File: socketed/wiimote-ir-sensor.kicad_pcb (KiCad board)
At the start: 2 copper layers, 13.5 x 16.2 mm, 10 parts, among them J1 Conn_01x04_Pin, U2 AP2112-3.3V, X1 SG3225CAN 24.0000M-TJGA3

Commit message: Socketed board: Tidy up
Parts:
- moved C1 22.8 mm to (158.2, 110.2)
- moved U1 22.0 mm to (156.8, 102.8)
- moved C3 22.0 mm to (152.0, 108.8)
- moved R1 22.0 mm to (154.8, 110.2)
- moved R2 22.0 mm to (156.5, 110.2)
- moved R3 22.0 mm to (161.0, 108.8)
- moved U2 22.0 mm to (151.9, 110.1)
- moved X1 22.0 mm to (159.5, 109.6)
- moved J1 21.7 mm to (152.9, 114.2)
- moved C2 21.7 mm to (152.0, 111.4)
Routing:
- net GND: track 30.5 -> 44.8 mm, vias 1 -> 6
- net +5V: track 11.7 -> 10.2 mm
- net /SCL: track 29.0 -> 27.7 mm
- net /CLK: track 17.2 -> 16.6 mm
- net /SDA: track 14.3 -> 14.7 mm, vias 2 -> 1

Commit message: More QoL tweaks to socketed board
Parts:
- R3: value 330K -> 33K
- moved J1 7.62 mm to (160.6, 114.2), turned to -90 degrees
- moved C1 0.25 mm to (158.5, 110.2)
- moved R1 0.25 mm to (154.5, 110.2)
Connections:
- J1 pad 1: +5V -> GND
- J1 pad 4: GND -> +5V
- R1 pad 2: /SDA -> /SCL
- R2 pad 1: /SCL -> /SDA
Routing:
- net /SCL: track 27.7 -> 30.5 mm, vias 0 -> 2
- net /SDA: track 14.7 -> 13.4 mm, vias 1 -> 2
- net GND: track 44.8 -> 43.9 mm

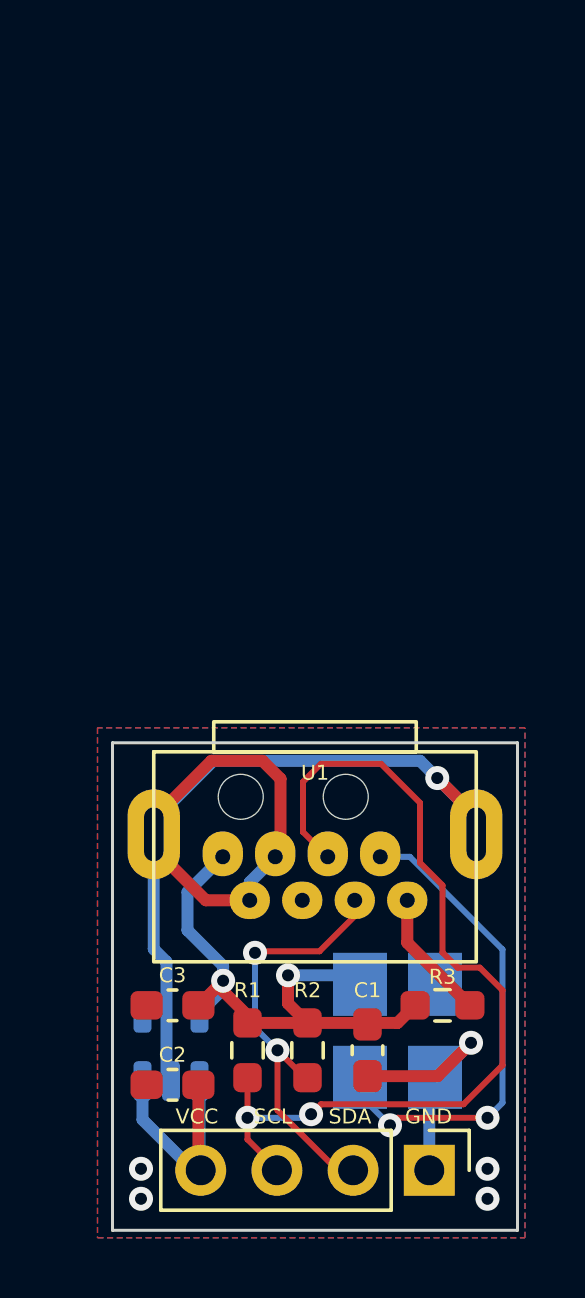
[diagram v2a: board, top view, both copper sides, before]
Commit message: Update socketed board - cleanup and add jumper to skip regulator
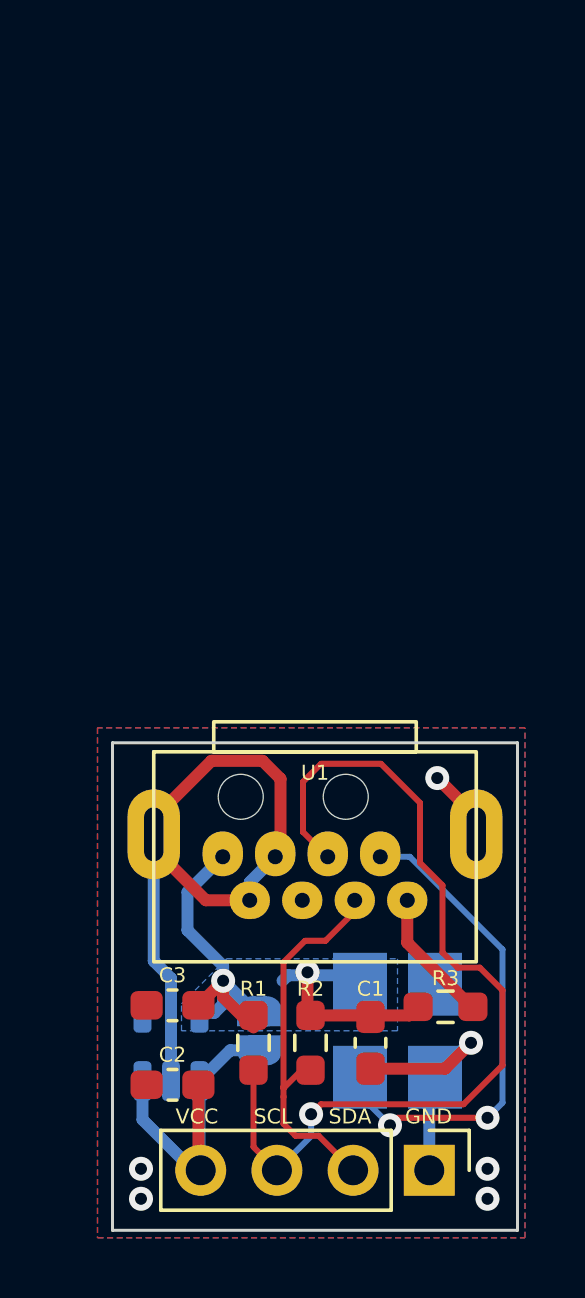
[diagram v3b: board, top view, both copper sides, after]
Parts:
- added JP1: SolderJumper_2_Open, Jumper:SolderJumper-2_P1.3mm_Open_RoundedPad1.0x1.5mm, B.Cu at (154.9, 109.6)
- moved R1 0.32 mm to (154.7, 110.0)
- moved C1 0.27 mm to (158.6, 110.0)
- moved R2 0.27 mm to (156.6, 110.0)
- moved R3 0.11 mm to (161.1, 108.8)
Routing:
- net GND: track 43.9 -> 31.9 mm
- net +5V: track 9.94 -> 12.6 mm
- net /SCL: track 30.5 -> 30.9 mm, vias 2 -> 1
- net /SDA: track 13.4 -> 13.1 mm, vias 2 -> 0
- added copper zone on B.Cu, net +3.3V
